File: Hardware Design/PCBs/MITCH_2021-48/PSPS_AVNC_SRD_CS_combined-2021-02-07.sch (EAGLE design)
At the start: 25 parts, among them U0-C STM32F411CEUX, U0-S TPS62202, U1-S ICM-20948

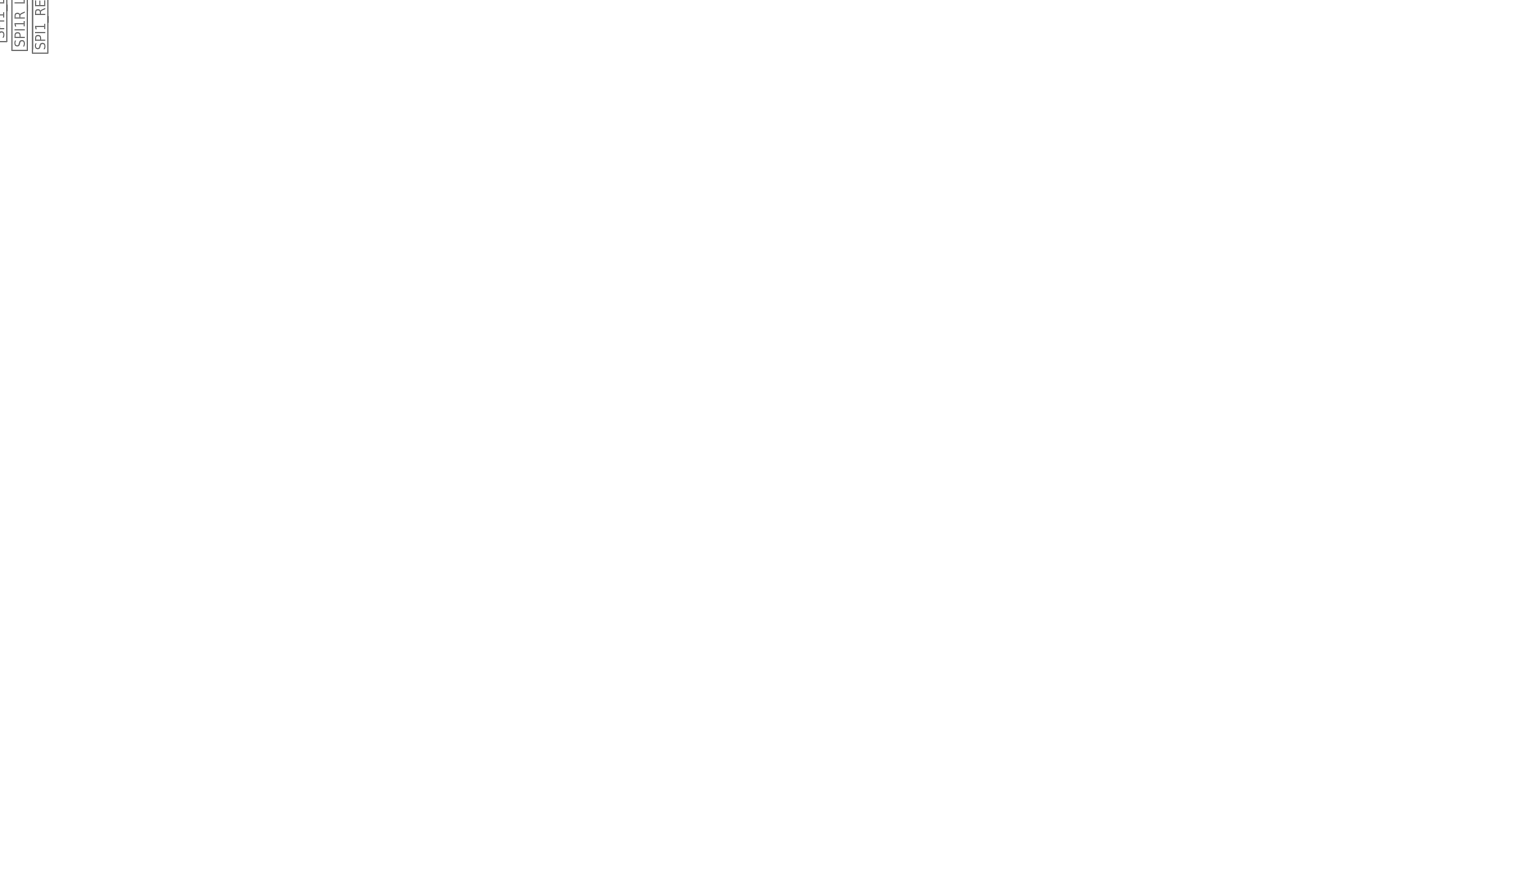
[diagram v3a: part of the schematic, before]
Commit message: Combined sensor block with processor block
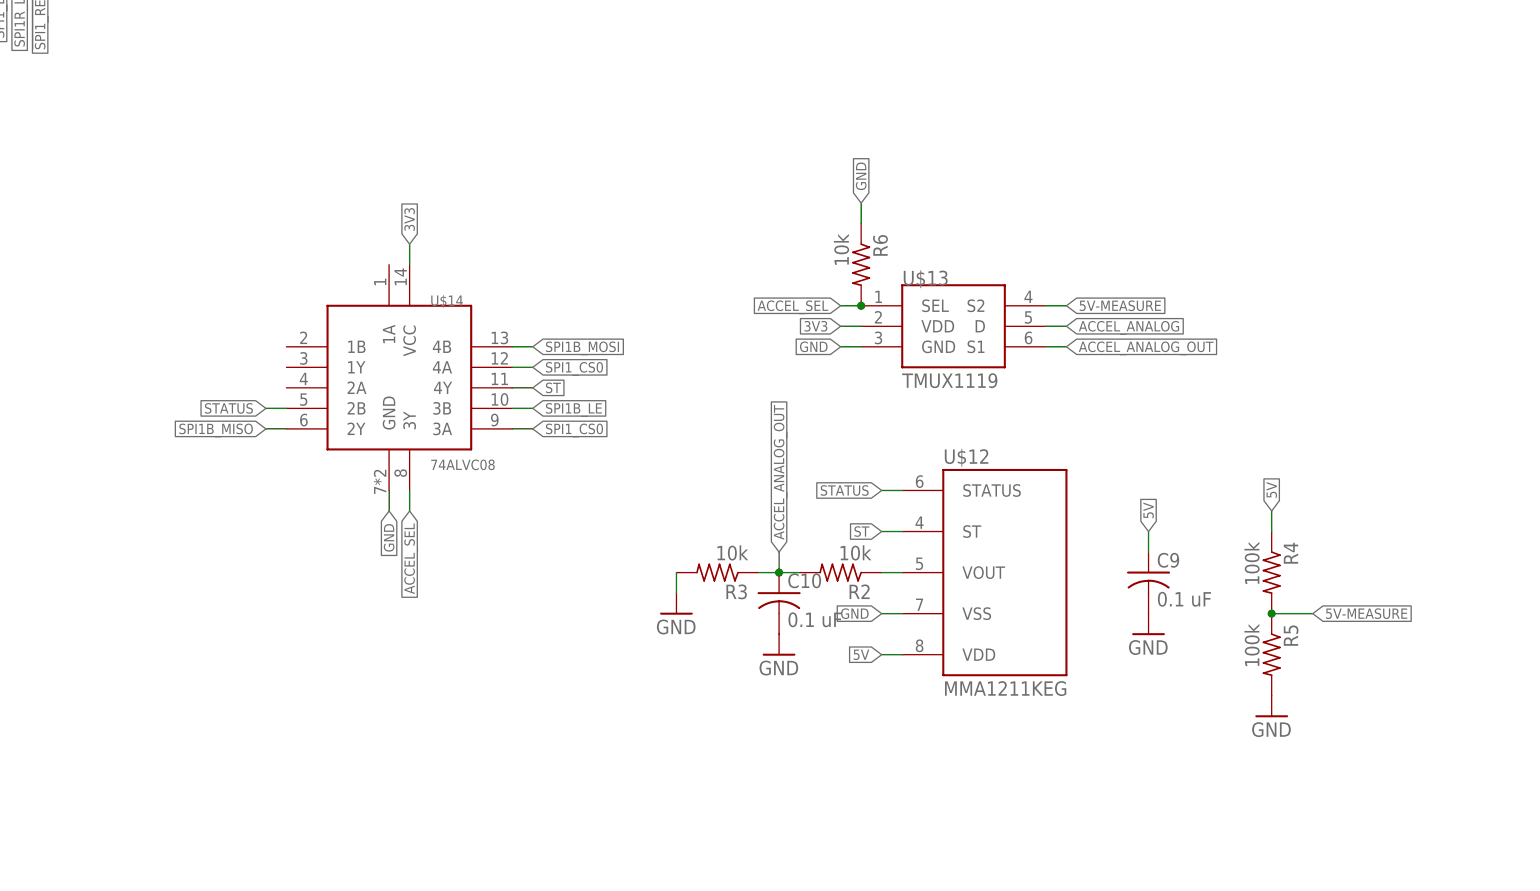
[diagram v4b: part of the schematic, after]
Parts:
- added C10, C9: 0.1 uF, resistor:C-USC0805
- added R2, R3, R6: 10k, resistor:R-US_M0805
- added R4, R5: 100k, resistor:R-US_M0805
- added U$12: MMA1211KEG, Computer2:MMA1211KEG
- added U$13: TMUX1119, Computer2:TMUX1119
- added U$14: 74ALVC08, Computer2:74ALVC08
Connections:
- new net 5V: C9.1, R4.1, U$12.VDD
- new net 5V-MEASURE: R4.2, R5.1, U$13.S2
- new net ACCEL_ANALOG_OUT: C10.1, R2.2, R3.1, U$13.S1
- new net ACCEL_SEL: R6.2, U$13.SEL, U$14.3Y
- new net ST: U$12.ST, U$14.4Y
- new net STATUS: U$12.STATUS, U$14.2B
- new net U0-S_VOUT: R2.1, U$12.VOUT
- net 3V3: now also U$13.VDD, U$14.VCC
- net ACCEL_ANALOG: now also U$13.D
- net GND: now also C10.2, C9.2, R3.2, R5.2, R6.1, U$12.VSS, U$13.GND, U$14.GND
- net SPI1B_LE: now also U$14.3B
- net SPI1B_MISO: now also U$14.2Y
- net SPI1B_MOSI: now also U$14.4B
- net SPI1_CS0: now also U$14.3A, U$14.4A
